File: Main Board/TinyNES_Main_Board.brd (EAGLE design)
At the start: 124.5 x 104.1 mm, 113 parts, among them J1 VIDEO, J2 AUDIO, J3 TRRS, J4 USB-C, Q1 PNP, U1 BUFFER, U10 74X1G74, U11 NCS603, U12 74X373, U13 RP2A03, U14 74X139, U15 RP2C02, U16 74X240, U17 BUFFER, U18 APX811, U19 FPF2107, U2 AP2138N, U3 SIT2001B, U4 ICS501, U5 BUFFER, U6 2KB, U7 2KB, U8 PL133-37, U9 74X1G74

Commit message: Main board revisions for production version
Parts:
- removed DA6: DA4-CA-SOT-363, TinyNES_Library:SOT-363-NP
- removed R25: 5.1k, TinyNES_Library:0805-NP
- added P1: 100k, TinyNES_Library:POT-3361
- added RGB: RGB-TOP, TinyNES_Library:RGB-TOP
- added S4: SPDT-EG1213, TinyNES_Library:EG1213
- added S5: SPDT-CUS-12TB, TinyNES_Library:CUS-12TB
- added U20: FPF2107, TinyNES_Library:SOT-23-5
- added U21: NOR, TinyNES_Library:SOT-23-5
- added U22: XOR, TinyNES_Library:SOT-23-5
- C1: value 0.1u -> 1u
- C22: value 330p -> 10u; device TinyNES_Library:0805-NP -> TinyNES_Library:1206-P
- C23: value 10u -> 330p; device TinyNES_Library:1206-P -> TinyNES_Library:0805-NP
- C24: value 330p -> 0.1u
- C25: value 0.1u -> DNP
- C3: value 1u -> 0.1u
- C4: value 0.1u -> 10n
- C6: value 10n -> 0.1u
- DA5: value DA4-CK-SOT-363 -> DA2-S; device TinyNES_Library:SOT-363-NP -> TinyNES_Library:SOT-23-3
- R11: value 68k -> 12k
- R16, R17, R2: value 6.8k -> 10k
- R19: value 6.8k -> 300R
- R20: value 300R -> 270R
- R21: value 270R -> 110R
- R22: value 110R -> 150R
- R23: value 150R -> 5.1k
- S1: value DPDT -> DPDT-LONG
- S2: value SWITCH -> DPDT; device TinyNES_Library:TL1105 -> TinyNES_Library:JS202011J
- S3: value SPDT -> SWITCH; device TinyNES_Library:EG1213 -> TinyNES_Library:TL1105
- U11: value NCS603 -> 74X1G74; device TinyNES_Library:TSSOP-14 -> TinyNES_Library:TSSOP-8
- U12: value 74X373 -> NCS603; device TinyNES_Library:SOIC-20 -> TinyNES_Library:TSSOP-14
- U13: value RP2A03 -> 74X373; device TinyNES_Library:DIP-40 -> TinyNES_Library:SOIC-20
- U14: value 74X139 -> RP2A03; device TinyNES_Library:SOIC-16 -> TinyNES_Library:DIP-40
- U15: value RP2C02 -> 74X139; device TinyNES_Library:DIP-40 -> TinyNES_Library:SOIC-16
- U16: value 74X240 -> RP2C02; device TinyNES_Library:SOIC-20 -> TinyNES_Library:DIP-40
- U17: value BUFFER -> 74X240; device TinyNES_Library:SOT-23-5 -> TinyNES_Library:SOIC-20
- U18: value APX811 -> BUFFER; device TinyNES_Library:SOT-143 -> TinyNES_Library:SOT-23-5
- U19: value FPF2107 -> APX811; device TinyNES_Library:SOT-23-5 -> TinyNES_Library:SOT-143
- U2: value AP2138N -> SIT2001B; device TinyNES_Library:SOT-23-3 -> TinyNES_Library:SOT-23-5
- U3: value SIT2001B -> ICS501; device TinyNES_Library:SOT-23-5 -> TinyNES_Library:SOIC-8
- U4: value ICS501 -> BUFFER; device TinyNES_Library:SOIC-8 -> TinyNES_Library:SOT-23-5
- U5: value BUFFER -> 2KB; device TinyNES_Library:SOT-23-5 -> TinyNES_Library:SOIC-28
- U7: value 2KB -> PL133-37; device TinyNES_Library:SOIC-28 -> TinyNES_Library:SOT-23-6
- U8: value PL133-37 -> SIT2001B; device TinyNES_Library:SOT-23-6 -> TinyNES_Library:SOT-23-5
- U9: value 74X1G74 -> AP2138N; device TinyNES_Library:TSSOP-8 -> TinyNES_Library:SOT-23-3
- moved C24 90.6 mm to (105.2, 20.4), turned to 0 degrees
- moved U17 84.9 mm to (21.6, 21.6)
- moved U5 80.0 mm to (27.9, 75.6)
- moved S2 76.2 mm to (59.1, 78.7)
- moved U18 71.8 mm to (106.3, 15.9), turned to 90 degrees
- moved C2 68.6 mm to (17.1, 80.0)
- moved U6 68.6 mm to (96.5, 75.6)
- moved U19 65.9 mm to (34.5, 12.4), turned to 0 degrees
- moved S3 63.0 mm to (36.8, 5.84)
- moved U16 59.1 mm to (80.0, 30.5), turned to 270 degrees
- moved U15 56.1 mm to (24.1, 35.6), turned to 180 degrees
- moved U13 53.4 mm to (97.8, 58.4)
- moved R20 48.5 mm to (99.6, 16.5), turned to 0 degrees
- moved R21 47.9 mm to (51.7, 14.5)
- moved C3 45.4 mm to (85.7, 80.0)
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- renumbered H2 to H5, H3 to H6
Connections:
- new net B: RGB.B, U16.16
- new net G: RGB.G, U16.15
- new net N$14: P1.2, R11.1
- new net N$15: R16.1, U17.17, U17.8
- new net N$16: S1.BB, U8.4
- new net N$17: S1.BA, U2.4
- new net N$18: S1.ACOM, U7.3
- new net N$19: S1.AA, U2.5
- new net N$20: U21.4, U22.2
- new net N$21: S5.2, U16.12
- new net N$22: S5.3, U22.4
- new net R: RGB.R, U16.14
- net !IRQ: now also U14.32; no longer U13.32
- net !NMI: now also R17.1, U14.33, U16.19; no longer R18.1, U13.33, U15.19
- net !OE1: now also C21.2, U14.36, U17.1; no longer C22.2, R16.1, U13.36, U16.1
- net !OE2: now also U14.35, U17.19; no longer R19.1, U13.35, U16.19
- net !ROMSEL: now also U15.9; no longer U14.9
- net 1Y0-!CS: now also U15.4, U5.20; no longer U14.4, U6.20
- net 3V3: now also C1.1, C6.1, C8.1, S1.BCOM, U7.5, U9.2; no longer C4.1, C5.1, C7.1, U2.2, U3.4, U8.5
- net A0: now also S5.1, U14.4, U22.1, U5.10; no longer U13.4, U15.12, U6.10
- net A1: now also U14.5, U16.11, U21.1, U5.9; no longer U13.5, U15.11, U6.9
- net A10: now also U14.14, U5.21; no longer U13.14, U6.21
- net A11: now also U14.15; no longer U13.15
- net A12: now also U14.16; no longer U13.16
- net A13: now also U14.17, U15.2; no longer U13.17, U14.2
- net A14: now also U14.18, U15.3; no longer U13.18, U14.3
- net A15: now also U14.19, U15.13; no longer U13.19, U14.13
- net A2: now also U14.6, U16.10, U21.2, U5.8; no longer U13.6, U15.10, U6.8
- net A3: now also U14.7, U5.7; no longer U13.7, U6.7
- net A4: now also U14.8, U5.6; no longer U13.8, U6.6
- net A5: now also U14.9, U5.5; no longer U13.9, U6.5
- net A6: now also U14.10, U5.4; no longer U13.10, U6.4
- net A7: now also U14.11, U5.3; no longer U13.11, U6.3
- net A8: now also U14.12, U5.25; no longer U13.12, U6.25
- net A9: now also U14.13, U5.24; no longer U13.13, U6.24
- net ALE: now also U13.11, U16.39; no longer U12.11, U15.39
- net AUDIO-OUT: now also R22.2; no longer R23.2
- net AUDIO1: now also U14.1; no longer U13.1
- net AUDIO2: now also U14.2; no longer U13.2
- net CIC: now also U4.4; no longer U5.4
- net CLK: now also S1.AB, U8.5; no longer U3.5, U8.3
- net CLK0: now also U7.4; no longer U8.4
- net CLK1: now also U7.1; no longer U8.1
- net CLK2: now also U7.6; no longer U8.6
- net CLK5X: now also U10.1, U3.5; no longer U4.5, U9.1
- net CLK5X/2: now also U10.5, U11.1; no longer U10.1, U9.5
- net CLKIN: now also S2.BB, U3.1; no longer S1.BB, U4.1
- net CLKVCC: now also C4.2, C7.1, S2.ACOM, U11.6, U11.7, U11.8, U3.2, U3.6, U3.7; no longer C6.2, C8.1, S1.ACOM, U4.2, U4.6, U4.7, U9.6, U9.7, U9.8
- net CPUCLK: now also S2.BA, U11.5, U14.29; no longer S1.BA, U10.5, U13.29
- net CPUCLK-SW: now also S2.BCOM; no longer S1.BCOM
- net D0: now also U14.28, U16.2, U17.18, U17.9, U5.11; no longer U13.28, U15.2, U16.18, U16.9, U6.11
- net D1: now also U14.27, U16.3, U17.12, U17.3, U5.12; no longer U13.27, U15.3, U6.12
- net D2: now also U14.26, U16.4, U5.13; no longer U13.26, U15.4, U6.13
- net D3: now also U14.25, U16.5, U17.16, U17.7, U5.15; no longer U13.25, U15.5, U16.16, U16.7, U6.15
- net D4: now also U14.24, U16.6, U17.14, U17.5, U5.16; no longer U13.24, U15.6, U16.14, U16.5, U6.16
- net D5: now also U14.23, U16.7, U5.17; no longer U13.23, U15.7, U6.17
- net D6: now also U14.22, U16.8, U5.18; no longer U13.22, U15.8, U6.18
- net D7: now also U14.21, U16.9, U5.19; no longer U13.21, U15.9, U6.19
- net DQ1: now also U10.2, U10.3; no longer U9.2, U9.3
- net DQ2: now also U11.2, U11.3; no longer U10.2, U10.3
- net EXP6-OUT: now also P1.3, U12.12; no longer R11.1, U11.12
- net G1-2Y1: now also U15.1, U15.11; no longer U14.1, U14.11
- net GND: now also C22.N, C23.1, C24.2, C25.1, C4.1, C6.2, R23.1, RGB.GND@1, RGB.GND@2, S2.AA, S3.2, S4.3, U12.14, U12.4, U13.1, U13.10, U14.20, U14.30, U15.8, U16.20, U17.10, U18.3, U19.1, U20.2, U21.3, U22.3, U3.3, U3.4, U4.1, U5.14, U5.2, U5.22, U5.23, U5.26, U8.1, U9.1; no longer C22.1, C23.N, C24.1, C25.2, C4.2, C6.1, DA5.2, DA6.3, DA6.6, R25.1, S1.AA, S2.2, S3.3, U11.1, U11.10, U11.14, U13.20, U13.30, U14.15, U14.8, U15.14, U15.16, U15.17, U15.20, U16.10, U16.8, U17.1, U17.3, U19.2, U3.1, U4.4, U5.3, U6.22, U7.1, U7.14, U7.23, U7.26, U8.2, U9.4
- net LEDA: now also R20.1; no longer R21.1
- net LEDK: now also U18.4; no longer U17.4
- net M2: now also U14.31, U15.14; no longer U13.31, U14.14
- net N$1: now also R19.2; no longer R20.2
- net N$10: now also R22.1, U12.3; no longer R23.1, U11.3
- net N$13: now also U12.7; no longer U11.7
- net N$2: now also R24.2; no longer R25.2
- net N$3: now also R23.2; no longer R24.2
- net N$4: now also U12.8; no longer U11.8
- net N$5: now also R21.1; no longer R22.1
- net N$6: now also R21.2, RGB.S; no longer R22.2
- net N$7: now also U12.13; no longer U11.13
- net N$8: now also U12.2; no longer U11.2
- net N$9: now also U12.6; no longer U11.6
- net OUT0: now also DA5.3, R18.1, U14.39; no longer C21.2, DA5.4, DA5.5, DA6.4, DA6.5, R17.1, U13.39
- net P1-D0: now also U17.2; no longer U16.2
- net P1-D3: now also U17.4; no longer U16.4
- net P1-D4: now also U17.6; no longer U16.6
- net P2-D0: now also U17.11; no longer U16.11
- net P2-D3: now also C23.2, U17.13; no longer C24.2, U16.13
- net P2-D4: now also U17.15; no longer U16.15
- net PA0: now also U13.19, U6.10; no longer U12.19, U7.10
- net PA1: now also U13.16, U6.9; no longer U12.16, U7.9
- net PA10: now also U16.28; no longer U15.28
- net PA11: now also U16.27; no longer U15.27
- net PA12: now also U16.26; no longer U15.26
- net PA13: now also U16.25; no longer U15.25
- net PA2: now also U13.15, U6.8; no longer U12.15, U7.8
- net PA3: now also U13.12, U6.7; no longer U12.12, U7.7
- net PA4: now also U13.9, U6.6; no longer U12.9, U7.6
- net PA5: now also U13.6, U6.5; no longer U12.6, U7.5
- net PA6: now also U13.5, U6.4; no longer U12.5, U7.4
- net PA7: now also U13.2, U6.3; no longer U12.2, U7.3
- net PA8: now also U16.30, U6.25; no longer U15.30, U7.25
- net PA9: now also U16.29, U6.24; no longer U15.29, U7.24
- net PD0: now also U13.18, U16.38, U6.11; no longer U12.18, U15.38, U7.11
- net PD1: now also U13.17, U16.37, U6.12; no longer U12.17, U15.37, U7.12
- net PD2: now also U13.14, U16.36, U6.13; no longer U12.14, U15.36, U7.13
- net PD3: now also U13.13, U16.35, U6.15; no longer U12.13, U15.35, U7.15
- net PD4: now also U13.8, U16.34, U6.16; no longer U12.8, U15.34, U7.16
- net PD5: now also U13.7, U16.33, U6.17; no longer U12.7, U15.33, U7.17
- net PD6: now also U13.4, U16.32, U6.18; no longer U12.4, U15.32, U7.18
- net PD7: now also U13.3, U16.31, U6.19; no longer U12.3, U15.31, U7.19
- net PPU-!CS: now also U15.5, U16.13; no longer U14.5, U15.13
- net PPU-!RD: now also C25.2, U16.24, U6.22; no longer U15.24, U7.22
- net PPU-!WR: now also U16.23, U6.27; no longer U15.23, U7.27
- net PPUCLK: now also U16.18; no longer U15.18
- net PWR-ON: now also S4.2, U20.3; no longer S3.2, U19.3
- net R/!W: now also U14.34, U16.1, U5.27; no longer U13.34, U15.1, U6.27
- net RESET: now also U14.3, U16.22, U19.2, U4.2; no longer U13.3, U15.22, U17.2, U5.2
- net RESET-SW: now also S3.1, U19.3; no longer S2.1, U18.3
- net VCC: now also C22.P, C24.1, C5.1, DA5.2, R19.1, R20.2, RGB.VCC@1, RGB.VCC@2, RGB.VCC@3, S2.AB, U12.11, U12.5, U12.9, U13.20, U14.40, U15.16, U16.40, U17.20, U18.5, U19.4, U20.5, U21.5, U22.5, U4.5, U5.28, U9.3; no longer C1.1, C23.P, C25.1, DA5.3, DA5.6, DA6.1, DA6.2, R19.2, R20.1, R21.2, S1.AB, U11.11, U11.5, U11.9, U12.20, U13.40, U14.16, U15.40, U16.20, U17.5, U18.4, U19.5, U2.3, U5.5, U7.28
- net VIDEO: now also U16.21; no longer U15.21
- net VIN: now also S4.1, U20.1; no longer S3.1, U19.1
- net VRAM-!CS: now also U6.20; no longer U7.20
- net VRAM-A10: now also U6.21; no longer U7.21
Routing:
- net N$14: track 0.00 -> 68.4 mm, vias 0 -> 3
- net D1: track 126.1 -> 182.9 mm, vias 2 -> 6
- net EXP6-OUT: track 106.0 -> 154.8 mm
- net A0: track 105.0 -> 146.4 mm, vias 2 -> 5
- net R: track 0.00 -> 38.7 mm, vias 0 -> 1
- net N$21: track 0.00 -> 34.3 mm, vias 0 -> 1
- net G: track 0.00 -> 32.9 mm, vias 0 -> 1
- net N$15: track 0.00 -> 29.6 mm, vias 0 -> 3
- net B: track 0.00 -> 27.9 mm, vias 0 -> 1
- net VCC: track 482.9 -> 506.1 mm
- net N$18: track 0.00 -> 20.9 mm
- net 3V3: track 12.1 -> 32.4 mm
- net !OE1: track 111.4 -> 92.3 mm, vias 6 -> 5
- net A1: track 106.5 -> 124.6 mm, vias 2 -> 3
- net OUT0: track 93.1 -> 78.2 mm, vias 6 -> 3
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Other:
- outline, holes or cut-outs redrawn
- board text added: "2"
- board text added: "2022-07-12"
- board text added: "2C05"
- board text added: "5V"
- board text added: "B"
- board text added: "G"
- board text added: "GND"
- board text added: "H2"
- board text added: "H3"
- board text added: "H4"
- board text added: "NTSC"
- board text added: "PAL"
- board text added: "R"
- board text added: "REG"
- board text added: "Revision Y"
- board text added: "S"
- board text added: "TD-TNES-Y-MB"
- board text added: "TinyNES Main Board TD-TNES-Y-MB 2022-07-12 tall-dog.com"
- board text added: "U"
- board text removed: "2022-03-08"
- board text removed: "RP2A03 / UA6527 ↓"
- board text removed: "RP2C02 / UA6528 ↓"
- board text removed: "Revision T"
- board text removed: "TD-TNES-T-MB"
- board text removed: "TinyNES Main Board TD-TNES-T-MB 2022-03-08 tall-dog.com"

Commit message: Minor cleanup
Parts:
- H1: value CART-72 -> CART
- U14: value RP2A03 -> CPU
- U16: value RP2C02 -> PPU
- U20: value FPF2107 -> FPF210X
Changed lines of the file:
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@@
 <attribute name="NAME" x="75.438" y="79.121" size="1" layer="51" ratio="10" rot="R180" align="center"/>
 </element>
-<element name="H1" library="TinyNES_Library" package="CART-72-2.50-CONN-VERT" value="CART-72" x="62.23" y="93.98" smashed="yes" rot="R180">
+<element name="H1" library="TinyNES_Library" package="CART-72-2.50-CONN-VERT" value="CART" x="62.23" y="93.98" smashed="yes" rot="R180">
 <attribute name="NAME" x="62.23" y="93.98" size="1" layer="51" ratio="10" rot="R180" align="center"/>
 <attribute name="NAME" x="13.208" y="89.027" size="1" layer="21" ratio="10" align="top-left"/>
 </element>
-<element name="U14" library="TinyNES_Library" package="DIP-40" value="RP2A03" x="44.45" y="55.88" smashed="yes" rot="R270">
+<element name="U14" library="TinyNES_Library" package="DIP-40" value="CPU" x="44.45" y="55.88" smashed="yes" rot="R270">
 <attribute name="NAME" x="70.358" y="61.087" size="1" layer="21" ratio="10" rot="R90" align="top-center"/>
 <attribute name="NAME" x="44.45" y="55.88" size="1" layer="51" ratio="10" align="center"/>
 </element>
-<element name="U16" library="TinyNES_Library" package="DIP-40" value="RP2C02" x="80.01" y="30.48" smashed="yes" rot="R270">
+<element name="U16" library="TinyNES_Library" package="DIP-40" value="PPU" x="80.01" y="30.48" smashed="yes" rot="R270">
 <attribute name="NAME" x="105.791" y="36.83" size="1" layer="21" ratio="10" rot="R90" align="top-center"/>
 <attribute name="NAME" x="80.01" y="30.48" size="1" layer="51" ratio="10" align="center"/>
@@
 <element name="HOLE1" library="TinyNES_Library" package="HOLE-M2.5" value="HOLE-M2.5" x="4.7244" y="93.98" smashed="yes"/>
 <element name="HOLE7" library="TinyNES_Library" package="HOLE-M2.5" value="HOLE-M2.5" x="70.485" y="15.875" smashed="yes"/>
-<element name="U20" library="TinyNES_Library" package="SOT-23-5" value="FPF2107" x="100.203" y="6.731" smashed="yes" rot="R270">
+<element name="U20" library="TinyNES_Library" package="SOT-23-5" value="FPF210X" x="100.203" y="6.731" smashed="yes" rot="R270">
 <attribute name="NAME" x="98.044" y="6.731" size="1" layer="21" ratio="10" rot="R270" align="top-center"/>
 <attribute name="NAME" x="100.203" y="6.731" size="1" layer="51" ratio="10" rot="R270" align="center"/>

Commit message: main board version updates
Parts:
- H5: value CTRL -> CTRL1
- H6: value CTRL -> CTRL2
- J3: device TinyNES_Library:54-00174 -> TinyNES_Library:SJ-43514
- Q1: value PNP -> 3906
- moved R19 4.70 mm to (51.1, 22.6)
- moved Q1 3.07 mm to (51.7, 18.3), turned to 180 degrees
- moved R21 0.25 mm to (51.7, 14.7)
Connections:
- new net EXT3: RGB.EXT3, U16.17
- net AUDIO1-OUT: now also J3.2; no longer J3.4AB, J3.4AT, J3.4BB, J3.4BT
- net AUDIO2-OUT: now also J3.3; no longer J3.3B, J3.3T
- net GND: now also J3.1, RGB.GND; no longer J3.1B, J3.1T, RGB.GND@1, RGB.GND@2, U16.17
- net N$12: now also J3.4; no longer J3.2B, J3.2T
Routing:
- net EXT3: track 0.00 -> 36.5 mm, vias 0 -> 1
- net N$12: track 4.25 -> 18.3 mm
- net AUDIO1-OUT: track 19.2 -> 7.74 mm
- net VCC: track 506.1 -> 501.4 mm, vias 23 -> 22
- net AUDIO2-OUT: track 3.28 -> 6.83 mm
- net N$1: track 9.41 -> 8.90 mm
- net GND: vias 823 -> 835
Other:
- outline, holes or cut-outs redrawn
- board text added: "(USE J3 SPACER)"
- board text added: "2023-03-02"
- board text added: "EX3"
- board text added: "PWR"
- board text added: "Revision Z"
- board text added: "TD-TNES-Z-MB"
- board text added: "TinyNES Main Board TD-TNES-Z-MB 2022-03-02 tall-dog.com"
- board text added: "USE J3 SPACER"
- board text removed: "2022-07-12"
- board text removed: "POWER"
- board text removed: "Revision Y"
- board text removed: "TD-TNES-Y-MB"
- board text removed: "TinyNES Main Board TD-TNES-Y-MB 2022-07-12 tall-dog.com"

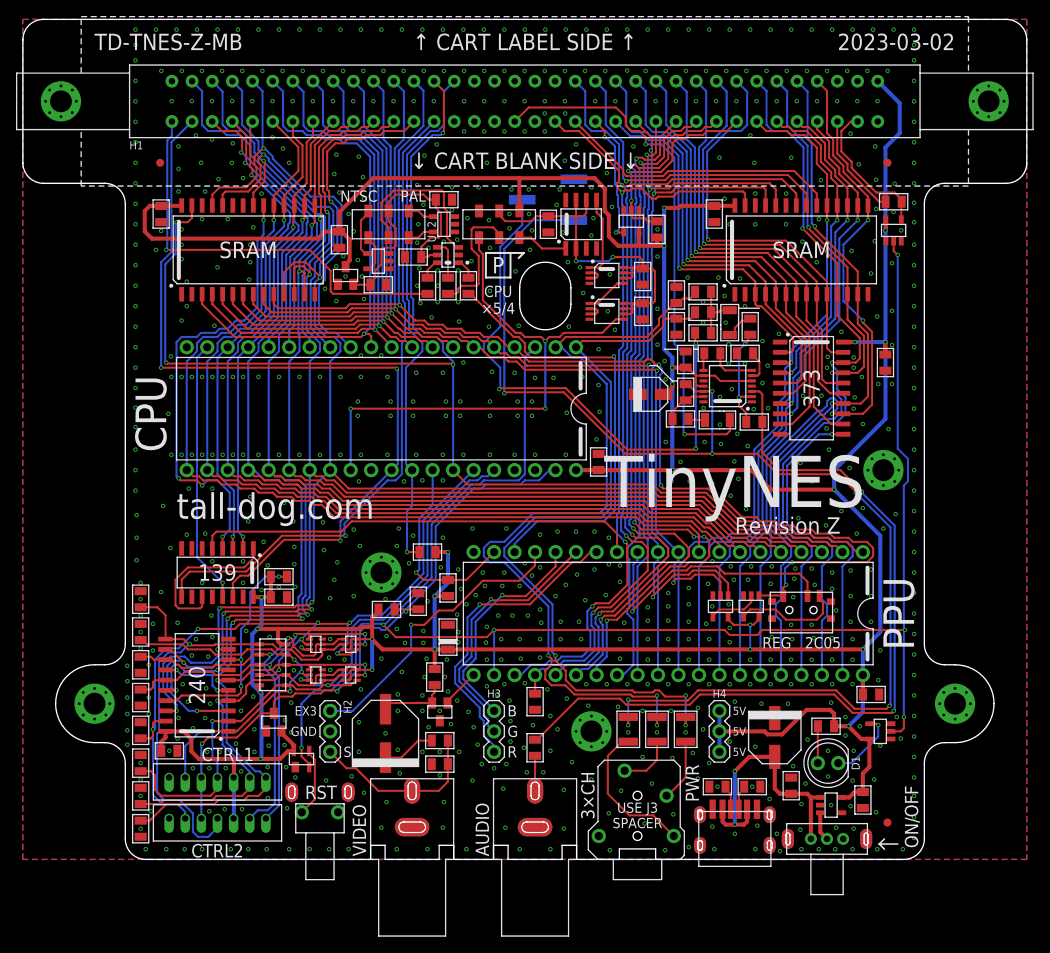
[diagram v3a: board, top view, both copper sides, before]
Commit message: Updates in preparation for next production run (Main Board Rev 27)
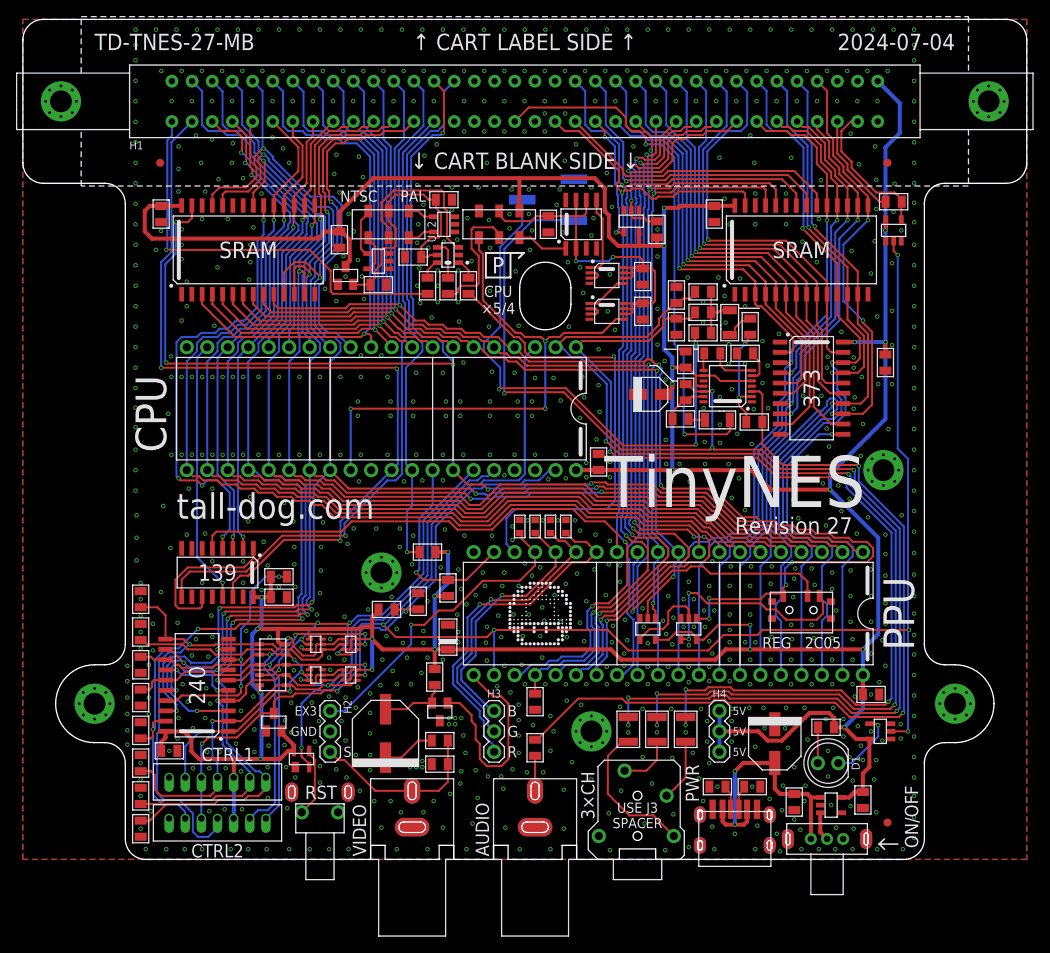
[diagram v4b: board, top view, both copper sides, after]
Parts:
- added R25, R26, R27, R28: 1M, TinyNES_Library:0603-NP
- added U$1: (no value), TinyNES_Library:_PIXEL-ART-1UP
- added U$2: (no value), TinyNES_Library:_PIXEL-ART-LEAF
- moved U21 9.44 mm to (77.5, 28.6)
- moved U22 8.24 mm to (82.5, 28.6)
- moved C36 2.07 mm to (95.6, 7.11), turned to 90 degrees
- moved C32 0.76 mm to (93.2, 14.4)
- moved R20 0.13 mm to (99.6, 16.4)
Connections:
- net AUDIO-MIX1 renamed AUDIO-MIX-1
- net AUDIO-OUT renamed AUDIO-MIX-AC
- net AUDIO1 renamed AUDIO1-DC
- net AUDIO1-OUT renamed AUDIO1-AC
- net AUDIO2 renamed AUDIO2-DC
- net AUDIO2-OUT renamed AUDIO2-AC
- net CLK renamed CLK-NTSC
- net EXP6-OUT renamed EXP6-DC
- net N$1 renamed VIDEO1
- net N$10 renamed AUDIO-MIX-DC
- net N$11 renamed EXP6-1
- net N$12 renamed EXP6-AC
- net N$13 renamed CN
- net N$14 renamed EXP6-MIX
- net N$15 renamed D1-PULLUP
- net N$16 renamed VDD-NTSC
- net N$17 renamed VDD-PAL
- net N$18 renamed CLK-FIN
- net N$19 renamed CLK-PAL
- net N$2 renamed CC2
- net N$20 renamed A0-NOR
- net N$21 renamed A0-PPU
- net N$22 renamed A0-XOR
- net N$3 renamed CC1
- net N$4 renamed CP
- net N$5 renamed VIDEO2
- net N$6 renamed VIDEO-OUT
- net N$7 renamed EXP6-2
- net N$8 renamed AUDIO-MIX-2
- net N$9 renamed GND-CAP
- removed net B: RGB.B, U16.16
- removed net G: RGB.G, U16.15
- removed net R: RGB.R, U16.14
- new net RGB-BLUE: R26.2, RGB.B, U16.16
- new net RGB-GREEN: R27.2, RGB.G, U16.15
- new net RGB-RED: R28.2, RGB.R, U16.14
- net EXT3: now also R25.2
- net GND: now also R25.1, R26.1, R27.1, R28.1
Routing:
- net RGB-RED: track 0.00 -> 43.7 mm, vias 0 -> 1
- net R: track 38.7 -> 0.00 mm, vias 1 -> 0
- net RGB-GREEN: track 0.00 -> 37.2 mm, vias 0 -> 1
- net G: track 32.9 -> 0.00 mm, vias 1 -> 0
- net AUDIO2-DC: track 102.1 -> 134.8 mm, vias 3 -> 5
- net RGB-BLUE: track 0.00 -> 31.8 mm, vias 0 -> 1
- net AUDIO1-DC: track 94.3 -> 124.4 mm, vias 3 -> 5
- net B: track 27.9 -> 0.00 mm, vias 1 -> 0
- net VIDEO: track 4.81 -> 26.6 mm
- net A0-XOR: track 13.5 -> 27.4 mm, vias 0 -> 2
- net A0: track 146.4 -> 157.1 mm, vias 5 -> 7
- net A1: track 124.6 -> 114.3 mm
- net VCC: track 501.4 -> 511.1 mm
- net A0-NOR: track 6.46 -> 9.95 mm
- net EXP6-DC: track 154.8 -> 157.5 mm
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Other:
- board text added: "2024-07-04"
- board text added: "Revision 27"
- board text added: "TD-TNES-27-MB"
- board text added: "TinyNES Main Board TD-TNES-27-MB 2024-07-04 tall-dog.com"
- board text removed: "2023-03-02"
- board text removed: "Revision Z"
- board text removed: "TD-TNES-Z-MB"
- board text removed: "TinyNES Main Board TD-TNES-Z-MB 2022-03-02 tall-dog.com"

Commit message: minor resistor component value change
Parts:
- R25, R26, R27, R28: value 1M -> 10k
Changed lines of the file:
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@@
 <element name="U$1" library="TinyNES_Library" package="_PIXEL-ART-1UP" value="" x="64.135" y="30.48" smashed="yes"/>
 <element name="U$2" library="TinyNES_Library" package="_PIXEL-ART-LEAF" value="" x="29.21" y="55.499" smashed="yes"/>
-<element name="R28" library="TinyNES_Library" package="0603-NP" value="1M" x="67.31" y="41.275" smashed="yes" rot="R270">
+<element name="R28" library="TinyNES_Library" package="0603-NP" value="10k" x="67.31" y="41.275" smashed="yes" rot="R270">
 <attribute name="NAME" x="67.31" y="43.053" size="1" layer="21" ratio="10" rot="R90" align="center-left"/>
 <attribute name="NAME" x="67.31" y="41.275" size="0.75" layer="51" font="vector" ratio="12" rot="R270" align="center"/>
 </element>
-<element name="R27" library="TinyNES_Library" package="0603-NP" value="1M" x="65.405" y="41.275" smashed="yes" rot="R270">
+<element name="R27" library="TinyNES_Library" package="0603-NP" value="10k" x="65.405" y="41.275" smashed="yes" rot="R270">
 <attribute name="NAME" x="65.405" y="43.053" size="1" layer="21" ratio="10" rot="R90" align="center-left"/>
 <attribute name="NAME" x="65.405" y="41.275" size="0.75" layer="51" font="vector" ratio="12" rot="R270" align="center"/>
 </element>
-<element name="R26" library="TinyNES_Library" package="0603-NP" value="1M" x="63.5" y="41.275" smashed="yes" rot="R270">
+<element name="R26" library="TinyNES_Library" package="0603-NP" value="10k" x="63.5" y="41.275" smashed="yes" rot="R270">
 <attribute name="NAME" x="63.5" y="43.053" size="1" layer="21" ratio="10" rot="R90" align="center-left"/>
 <attribute name="NAME" x="63.5" y="41.275" size="0.75" layer="51" font="vector" ratio="12" rot="R270" align="center"/>
 </element>
-<element name="R25" library="TinyNES_Library" package="0603-NP" value="1M" x="61.595" y="41.275" smashed="yes" rot="R270">
+<element name="R25" library="TinyNES_Library" package="0603-NP" value="10k" x="61.595" y="41.275" smashed="yes" rot="R270">
 <attribute name="NAME" x="61.595" y="43.053" size="1" layer="21" ratio="10" rot="R90" align="center-left"/>
 <attribute name="NAME" x="61.595" y="41.275" size="0.75" layer="51" ratio="12" rot="R270" align="center"/>
